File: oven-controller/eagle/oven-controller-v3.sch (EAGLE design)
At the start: 48 parts, among them Q1 FDV305N, Q2 FDV305N, Q3 FDV305N, Q4 FDV305N, U1 ARDUINO_SHIELDLONGPADS, U2 MAX31855, U3 MAX31855, U4 MAX31855, U5 MAX31855, U6 MAX31855

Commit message: Lots of fixes. Reviewed. Passes ERC, DRC, rats. Ship it.
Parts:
- added C11, C12, C13, C14: 10n, rcl_custom:C-EUC0603K
- added R10: 1k, rcl_custom:R-US_0603-C-NOSILK
- C10, C6, C8, C9: value 100n -> 100n 100V
- C7: value 100n -> 10n
- FAN: value HDR4 -> (none); device SparkFun-Connectors:M023.5MM_LOCK -> con-phoenix-254:MPT2
- HEAT1: value HDR2 -> (none); device SparkFun-Connectors:M023.5MM_LOCK -> con-phoenix-254:MPT2
- HEAT2: value HDR3 -> (none); device SparkFun-Connectors:M023.5MM_LOCK -> con-phoenix-254:MPT2
- R5, R7, R8, R9: value 330 -> 1k
- R6: value 330 -> 10k
- START: value HDR1 -> (none); device SparkFun-Connectors:M023.5MM_LOCK -> con-phoenix-254:MPT2
- THERM1, THERM2, THERM3, THERM4, THERM5: device SparkFun-Connectors:M023.5MM_LOCK -> con-phoenix-254:MPT2
- U1: value ARDUINO_SHIELDLONGPADS -> ARDUINO_SHIELDNOHOLES; device SparkFun-Boards:ARDUINO_SHIELDLONGPADS -> SparkFun-Boards:ARDUINO_SHIELDNOHOLES
- VENT: value HDR5 -> (none); device SparkFun-Connectors:M023.5MM_LOCK -> con-phoenix-254:MPT2
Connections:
- net CS_FAN renamed FAN_EN
- net CS_HEAT1 renamed HEAT1_EN
- net CS_HEAT2 renamed HEAT2_EN
- net CS_VENT renamed VENT_EN
- net THERM_CS1 renamed THERM_!CS1
- net THERM_CS2 renamed THERM_!CS2
- net THERM_CS3 renamed THERM_!CS3
- net THERM_CS4 renamed THERM_!CS4
- net THERM_CS5 renamed THERM_!CS5
- removed net N$11: THERM2.2, U3.T+
- removed net N$14: THERM4.1, U5.T-
- removed net N$16: THERM5.1, U6.T-
- removed net START: R6.1, START.1, U1.A0
- new net !START: LED1.C, R6.1, START-1.1, U1.A0
- new net N$1: LED1.A, R10.1
- new net N$10: C12.1, THERM3-1.1, U4.T-
- new net N$20: C12.2, THERM3-2.1, U4.T+
- net 12V: now also FAN-1.1, HEAT1-2.1, HEAT2-2.1, VENT-1.1; no longer FAN.1, HEAT1.1, HEAT2.1, VENT.1
- net 5V: now also R10.2; no longer C7.1
- net GND: now also START-2.1; no longer C7.2, LED1.C
- net HDR3: now also FAN-2.1; no longer FAN.2
- net N$12: now also C11.1, THERM2-1.1, U3.T-; no longer THERM3.1, U4.T-
- net N$13: now also C11.2, THERM2-2.1, U3.T+; no longer THERM3.2, U4.T+
- net N$15: now also C14.2, THERM5-2.1, U6.T+; no longer THERM4.2, U5.T+
- net N$17: now also C14.1, THERM5-1.1, U6.T-; no longer THERM5.2, U6.T+
- net N$2: now also C7.1, THERM1-1.1, U2.T-; no longer LED1.A, START.2
- net N$21: now also HEAT2-1.1; no longer HEAT2.2
- net N$3: now also VENT-2.1; no longer VENT.2
- net N$4: now also HEAT1-1.1; no longer HEAT1.2
- net N$5: now also C7.2, THERM1-2.1, U2.T+; no longer THERM1.1, U2.T-
- net N$6: now also C13.1, THERM4-1.1, U5.T-; no longer THERM1.2, U2.T+
- net N$8: now also C13.2, THERM4-2.1, U5.T+; no longer THERM2.1, U3.T-
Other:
- note added: "POWER IN FROM ARDUINO"
- moved on the sheet: C1, C10, C2, C3, C4, C5, C6, C7, C8, C9, D1, D2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

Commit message: Added level translators. Passes ERC, DRC. Needs review.
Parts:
- added U7, U8: (no value), SparkFun-DigitalIC:TXB0104PWR
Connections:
- removed net SPI_CLK: U1.D13, U2.SCK, U3.SCK, U4.SCK, U5.SCK, U6.SCK
- removed net SPI_MISO: U1.D12, U2.SO, U3.SO, U4.SO, U5.SO, U6.SO
- removed net THERM_!CS1: U1.TX, U2.!CS
- removed net THERM_!CS2: U1.D2, U3.!CS
- removed net THERM_!CS3: U1.*D3, U4.!CS
- removed net THERM_!CS4: U1.D7, U5.!CS
- removed net THERM_!CS5: U1.*D9, U6.!CS
- new net SPI_CLK_A: U2.SCK, U3.SCK, U4.SCK, U5.SCK, U6.SCK, U7.A2
- new net SPI_CLK_B: U1.D13, U7.B2
- new net SPI_MISO_A: U2.SO, U3.SO, U4.SO, U5.SO, U6.SO, U7.A1
- new net SPI_MISO_B: U1.D12, U7.B1
- new net THERM_!CS1_A: U2.!CS, U7.A3
- new net THERM_!CS1_B: U1.TX, U7.B3
- new net THERM_!CS2_A: U3.!CS, U7.A4
- new net THERM_!CS2_B: U1.D2, U7.B4
- new net THERM_!CS3_A: U4.!CS, U8.A3
- new net THERM_!CS3_B: U1.*D3, U8.B3
- new net THERM_!CS4_A: U5.!CS, U8.A2
- new net THERM_!CS4_B: U1.D7, U8.B2
- new net THERM_!CS5_A: U6.!CS, U8.A1
- new net THERM_!CS5_B: U1.*D9, U8.B1
- net 3.3V: now also U7.VCCA, U8.VCCA
- net 5V: now also U7.VCCB, U8.VCCB
- net GND: now also U7.GND, U8.GND
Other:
- note added: "NC"
- moved on the sheet: C1, C10, C11, C12, C13, C14, C2, C3, C4, C5, C6, C7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

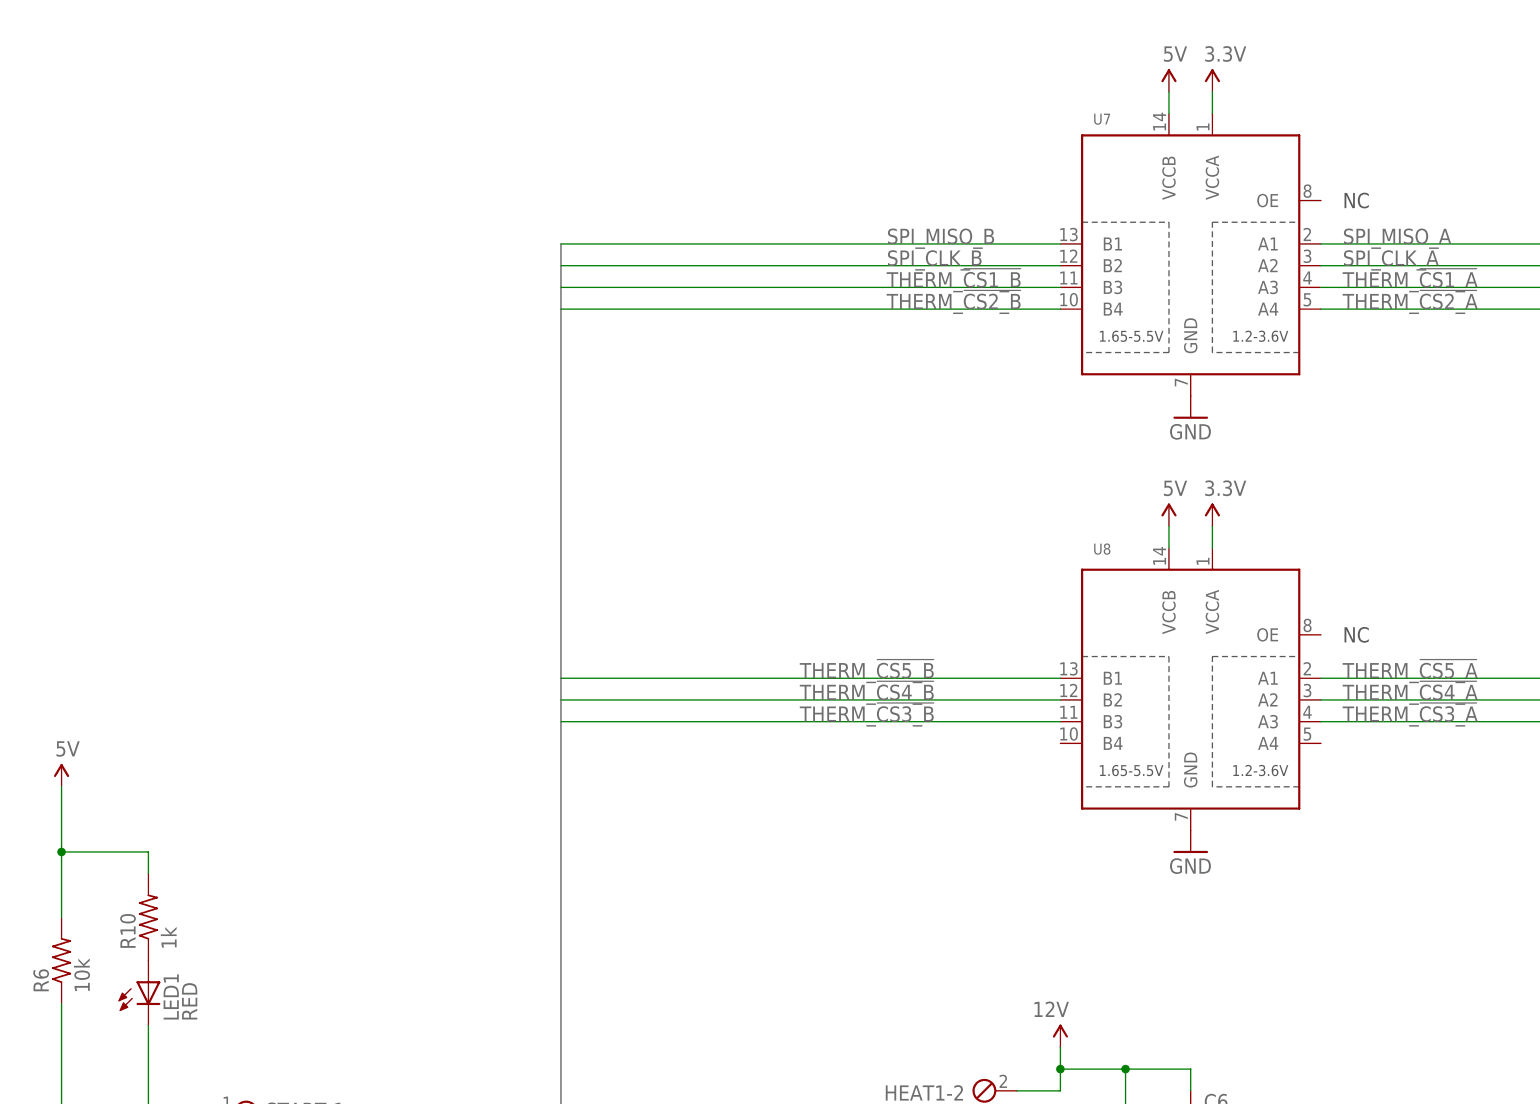
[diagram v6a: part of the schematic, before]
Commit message: Added v3.1 update to oven board.
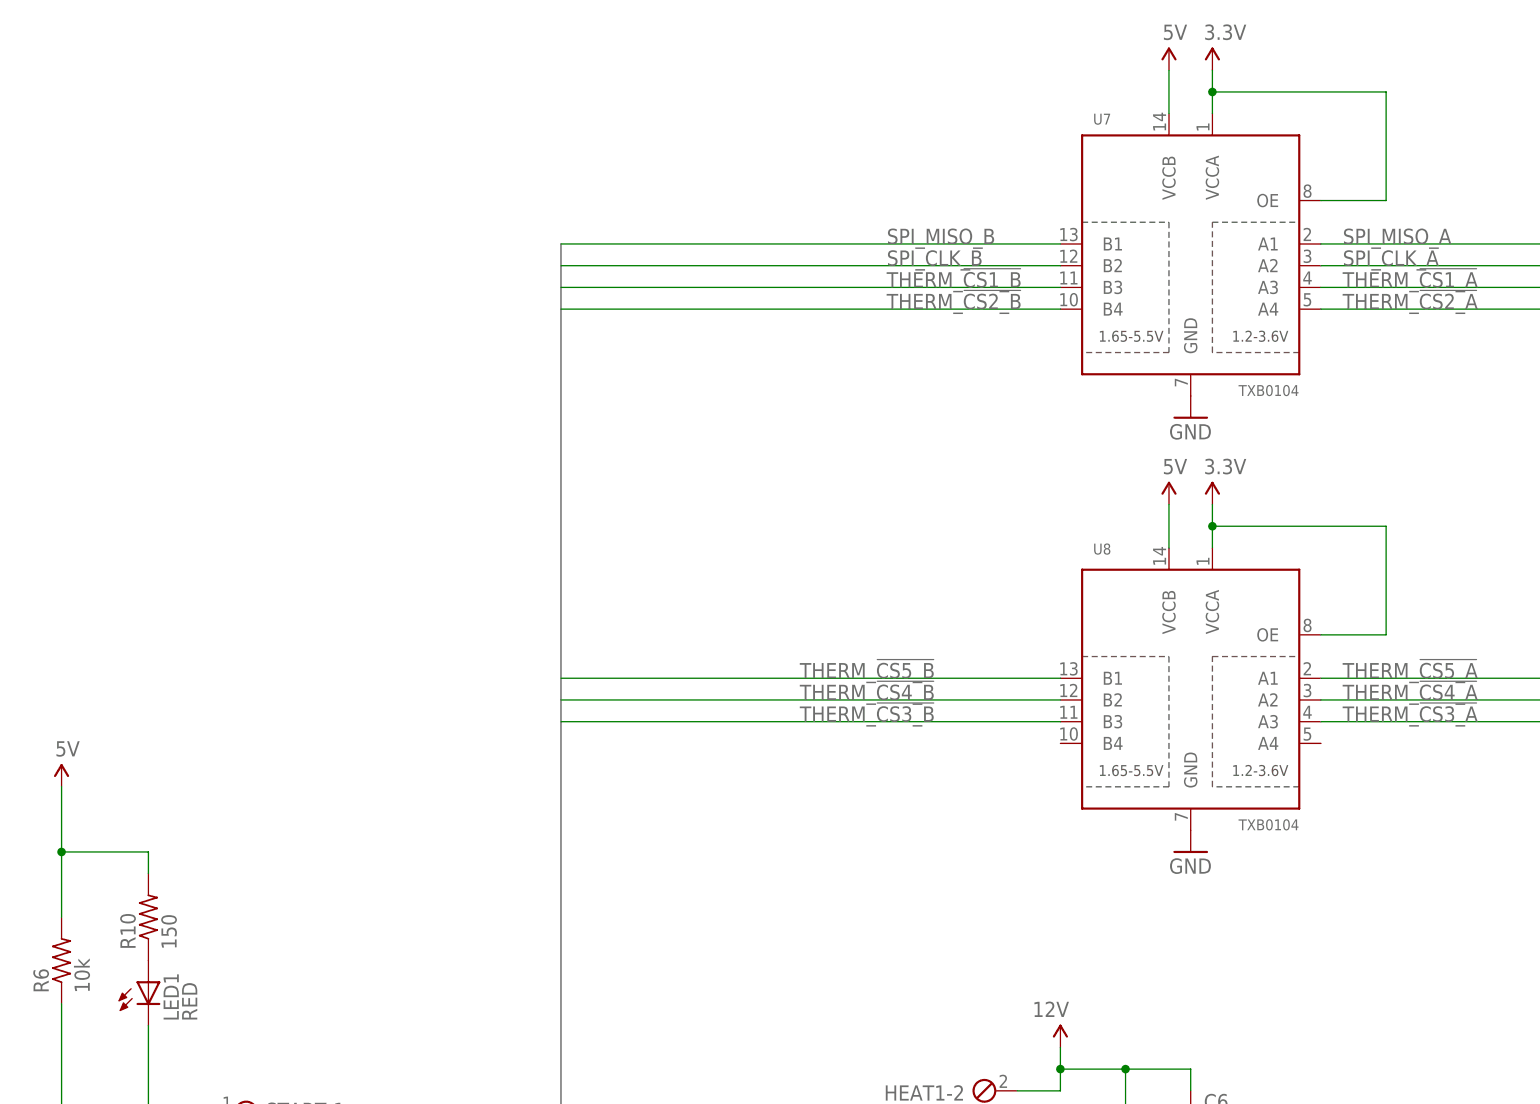
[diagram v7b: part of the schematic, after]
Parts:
- R10: value 1k -> 150
- U7, U8: value (none) -> TXB0104
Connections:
- net 3.3V: now also U7.OE, U8.OE
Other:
- note removed: "NC"
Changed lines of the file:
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@@
 <part name="FRAME1" library="frames" deviceset="FRAME_B_L" device=""/>
 <part name="U$4" library="SparkFun-Aesthetics" deviceset="VIN" device="" value="12V"/>
-<part name="R10" library="rcl_custom" deviceset="R-US_" device="0603-C-NOSILK" value="1k"/>
+<part name="R10" library="rcl_custom" deviceset="R-US_" device="0603-C-NOSILK" value="150"/>
 <part name="C7" library="rcl_custom" deviceset="C-EU" device="C0603K" value="10n"/>
 <part name="C11" library="rcl_custom" deviceset="C-EU" device="C0603K" value="10n"/>
@@
 <part name="THERM4" library="con-phoenix-254" deviceset="MPT2" device=""/>
 <part name="THERM5" library="con-phoenix-254" deviceset="MPT2" device=""/>
-<part name="U7" library="SparkFun-DigitalIC" deviceset="TXB0104PWR" device=""/>
-<part name="U8" library="SparkFun-DigitalIC" deviceset="TXB0104PWR" device=""/>
+<part name="U7" library="SparkFun-DigitalIC" deviceset="TXB0104PWR" device="" value="TXB0104"/>
+<part name="U8" library="SparkFun-DigitalIC" deviceset="TXB0104PWR" device="" value="TXB0104"/>
 <part name="U$5" library="SparkFun-Aesthetics" deviceset="5V" device=""/>
 <part name="U$6" library="SparkFun-Aesthetics" deviceset="5V" device=""/>
@@
 <wire x1="119.38" y1="71.12" x2="119.38" y2="91.44" width="0.1524" layer="97" style="longdash"/>
 <wire x1="119.38" y1="91.44" x2="81.28" y2="91.44" width="0.1524" layer="97" style="longdash"/>
-<text x="271.78" y="198.12" size="1.778" layer="97" align="center-left">NC</text>
-<text x="271.78" y="248.92" size="1.778" layer="97" align="center-left">NC</text>
 </plain>
 <instances>
@@
 <attribute name="VALUE" x="266.7" y="175.26" size="1.27" layer="96" rot="MR0"/>
 </instance>
-<instance part="U$5" gate="G$1" x="251.46" y="261.62"/>
-<instance part="U$6" gate="G$1" x="251.46" y="210.82"/>
-<instance part="P+7" gate="G$1" x="256.54" y="261.62"/>
-<instance part="P+8" gate="G$1" x="256.54" y="210.82"/>
+<instance part="U$5" gate="G$1" x="251.46" y="264.16"/>
+<instance part="U$6" gate="G$1" x="251.46" y="213.36"/>
+<instance part="P+7" gate="G$1" x="256.54" y="264.16"/>
+<instance part="P+8" gate="G$1" x="256.54" y="213.36"/>
 <instance part="GND1" gate="1" x="254" y="172.72"/>
 <instance part="GND8" gate="1" x="254" y="223.52"/>
@@
 <pinref part="U7" gate="G$1" pin="VCCB"/>
 <pinref part="U$5" gate="G$1" pin="5V"/>
-<wire x1="251.46" y1="261.62" x2="251.46" y2="259.08" width="0.1524" layer="91"/>
+<wire x1="251.46" y1="264.16" x2="251.46" y2="259.08" width="0.1524" layer="91"/>
 </segment>
 <segment>
 <pinref part="U8" gate="G$1" pin="VCCB"/>
 <pinref part="U$6" gate="G$1" pin="5V"/>
-<wire x1="251.46" y1="210.82" x2="251.46" y2="208.28" width="0.1524" layer="91"/>
+<wire x1="251.46" y1="213.36" x2="251.46" y2="208.28" width="0.1524" layer="91"/>
 </segment>
 </net>
@@
 <pinref part="U7" gate="G$1" pin="VCCA"/>
 <pinref part="P+7" gate="G$1" pin="3.3V"/>
+<wire x1="256.54" y1="264.16" x2="256.54" y2="261.62" width="0.1524" layer="91"/>
+<pinref part="U7" gate="G$1" pin="OE"/>
 <wire x1="256.54" y1="261.62" x2="256.54" y2="259.08" width="0.1524" layer="91"/>
+<wire x1="269.24" y1="248.92" x2="276.86" y2="248.92" width="0.1524" layer="91"/>
+<wire x1="276.86" y1="248.92" x2="276.86" y2="261.62" width="0.1524" layer="91"/>
+<wire x1="276.86" y1="261.62" x2="256.54" y2="261.62" width="0.1524" layer="91"/>
+<junction x="256.54" y="261.62"/>
 </segment>
 <segment>
 <pinref part="U8" gate="G$1" pin="VCCA"/>
 <pinref part="P+8" gate="G$1" pin="3.3V"/>
+<wire x1="256.54" y1="213.36" x2="256.54" y2="210.82" width="0.1524" layer="91"/>
+<pinref part="U8" gate="G$1" pin="OE"/>
 <wire x1="256.54" y1="210.82" x2="256.54" y2="208.28" width="0.1524" layer="91"/>
-</segment>
-</net>
+<wire x1="269.24" y1="198.12" x2="276.86" y2="198.12" width="0.1524" layer="91"/>
+<wire x1="276.86" y1="198.12" x2="276.86" y2="210.82" width="0.1524" layer="91"/>
+<wire x1="276.86" y1="210.82" x2="256.54" y2="210.82" width="0.1524" layer="91"/>
+<junction x="256.54" y="210.82"/>
+</segment>
+</net>
